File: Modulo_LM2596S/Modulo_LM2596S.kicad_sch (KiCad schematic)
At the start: 11 parts, among them U101 LM2596S-ADJ

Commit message: Footprint potenziometro (20/10/2022)
Ho assegnato la footprint al potenziometro, controllare se è corretto.
Il resto del circuito non è stato controllato
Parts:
- RV101: footprint (none) -> Potentiometer_THT:Potentiometer_Bourns_3299W_Vertical
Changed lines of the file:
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@@
       (effects (font (size 1.27 1.27)) (justify right))
     )
-    (property "Footprint" "" (id 2) (at 160.02 77.47 0)
+    (property "Footprint" "Potentiometer_THT:Potentiometer_Bourns_3299W_Vertical" (id 2) (at 160.02 77.47 0)
       (effects (font (size 1.27 1.27)) hide)
     )
@@
     )
     (path "/db17a703-a37d-4b79-9726-63333a30eb05"
-      (reference "RV101") (unit 1) (value "10k") (footprint "")
+      (reference "RV101") (unit 1) (value "10k") (footprint "Potentiometer_THT:Potentiometer_Bourns_3299W_Vertical")
     )
     (path "/329e714d-77d1-42d4-b688-ff586e973cc8"

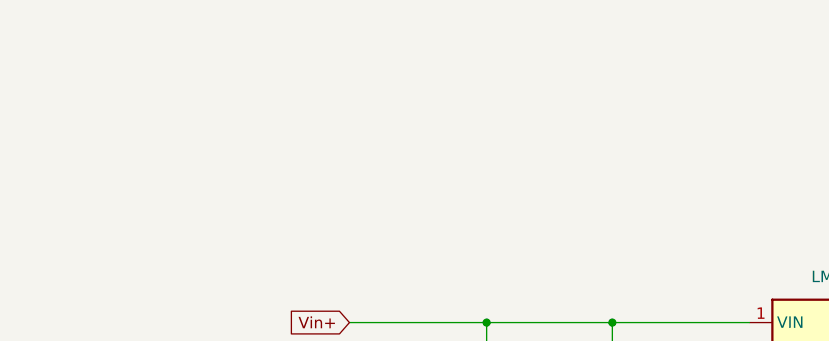
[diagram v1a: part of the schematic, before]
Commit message: Aggiunta di commento su potenziometro
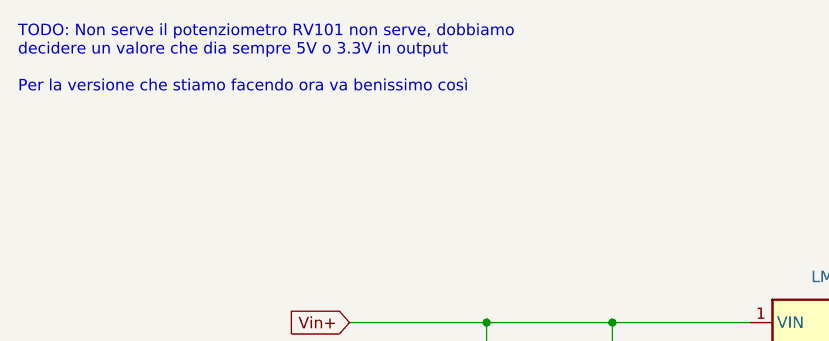
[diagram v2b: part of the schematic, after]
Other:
- note added: "TODO: Non serve il potenziometro RV101 non serve, dobbiamo decidere un valore che dia sempre 5V o 3.3V in output Per la versione che stiamo facendo ora va benissimo così"
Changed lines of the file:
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@@
     (stroke (width 0) (type default) (color 0 0 0 0))
+  )
+  (text "TODO: Non serve il potenziometro RV101 non serve, dobbiamo \ndecidere un valore che dia sempre 5V o 3.3V in output \n\nPer la versione che stiamo facendo ora va benissimo così"
+    (at 20.32 46.99 0)
+    (effects (font (size 1.27 1.27)) (justify left bottom))
   )
   (global_label "OUT+" (shape input) (at 193.04 73.66 0) (fields_autoplaced)

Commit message: Test delle metriche (22/10/2022)
Solo un test, non è finale o completo.
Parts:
- C101: footprint (none) -> Capacitor_SMD:CP_Elec_3x5.3
- C102: footprint (none) -> Capacitor_SMD:C_1812_4532Metric_Pad1.57x3.40mm_HandSolder
- R101: footprint (none) -> Resistor_SMD:R_0805_2012Metric_Pad1.20x1.40mm_HandSolder
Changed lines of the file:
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@@
       (effects (font (size 1.27 1.27)) (justify left))
     )
-    (property "Footprint" "" (id 2) (at 72.39 81.28 0)
+    (property "Footprint" "Capacitor_SMD:CP_Elec_3x5.3" (id 2) (at 72.39 81.28 0)
       (effects (font (size 1.27 1.27)) hide)
     )
@@
       (effects (font (size 1.27 1.27)) (justify left))
     )
-    (property "Footprint" "" (id 2) (at 158.242 86.36 90)
+    (property "Footprint" "Resistor_SMD:R_0805_2012Metric_Pad1.20x1.40mm_HandSolder" (id 2) (at 158.242 86.36 90)
       (effects (font (size 1.27 1.27)) hide)
     )
@@
       (effects (font (size 1.27 1.27)) (justify left))
     )
-    (property "Footprint" "" (id 2) (at 87.3252 85.09 0)
+    (property "Footprint" "Capacitor_SMD:C_1812_4532Metric_Pad1.57x3.40mm_HandSolder" (id 2) (at 87.3252 85.09 0)
       (effects (font (size 1.27 1.27)) hide)
     )
@@
     )
     (path "/36af99ba-44f3-4caf-a2f7-2f75678a02fb"
-      (reference "C101") (unit 1) (value "100uF") (footprint "")
+      (reference "C101") (unit 1) (value "100uF") (footprint "Capacitor_SMD:CP_Elec_3x5.3")
     )
     (path "/689c4dca-aa7d-493b-824b-0f528cf7fb1d"
-      (reference "C102") (unit 1) (value "1uF") (footprint "")
+      (reference "C102") (unit 1) (value "1uF") (footprint "Capacitor_SMD:C_1812_4532Metric_Pad1.57x3.40mm_HandSolder")
     )
     (path "/93b82181-0c21-4647-a6a8-8a9a0831c12f"
@@
     )
     (path "/664bdff7-aac1-4a8f-b1b1-4cc25c686d35"
-      (reference "R101") (unit 1) (value "330") (footprint "")
+      (reference "R101") (unit 1) (value "330") (footprint "Resistor_SMD:R_0805_2012Metric_Pad1.20x1.40mm_HandSolder")
     )
     (path "/8d177f27-30dc-4386-8473-ae66aa314cc6"

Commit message: Footprint (tentativo fallito)
23/10/2022 tentato di assegnare le footprint a tutti i componenti dello schema logico, ma senza successo
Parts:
- L101: footprint (none) -> Inductor_SMD:L_Bourns-SRU8028_8.0x8.0mm
- R102: footprint (none) -> Resistor_SMD:R_0805_2012Metric_Pad1.20x1.40mm_HandSolder
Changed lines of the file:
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@@
     (property "Reference" "L101" (id 0) (at 135.89 71.12 0))
     (property "Value" "47uH" (id 1) (at 135.89 73.66 0))
-    (property "Footprint" "" (id 2) (at 135.89 77.47 0)
+    (property "Footprint" "Inductor_SMD:L_Bourns-SRU8028_8.0x8.0mm" (id 2) (at 135.89 77.47 0)
       (effects (font (size 1.27 1.27)) hide)
     )
@@
       (effects (font (size 1.27 1.27)) (justify left))
     )
-    (property "Footprint" "" (id 2) (at 179.832 78.74 90)
+    (property "Footprint" "Resistor_SMD:R_0805_2012Metric_Pad1.20x1.40mm_HandSolder" (id 2) (at 179.832 78.74 90)
       (effects (font (size 1.27 1.27)) hide)
     )
@@
     )
     (path "/6d551d3c-151e-4aa5-b2c4-444cfcec29b2"
-      (reference "L101") (unit 1) (value "47uH") (footprint "")
+      (reference "L101") (unit 1) (value "47uH") (footprint "Inductor_SMD:L_Bourns-SRU8028_8.0x8.0mm")
     )
     (path "/664bdff7-aac1-4a8f-b1b1-4cc25c686d35"
@@
     )
     (path "/8d177f27-30dc-4386-8473-ae66aa314cc6"
-      (reference "R102") (unit 1) (value "1k") (footprint "")
+      (reference "R102") (unit 1) (value "1k") (footprint "Resistor_SMD:R_0805_2012Metric_Pad1.20x1.40mm_HandSolder")
     )
     (path "/db17a703-a37d-4b79-9726-63333a30eb05"

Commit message: LM2596S: creazione della scheda fisica
Selezione dei componenti e creazione del PCB.
TODO: Da mettere a posto le tracce @GiovanniRaseraF
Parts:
- removed D102: LED, symbol Device:LED
- removed R102: 1k, Resistor_SMD:R_0805_2012Metric_Pad1.20x1.40mm_HandSolder, symbol Device:R
- C101: footprint Capacitor_SMD:CP_Elec_3x5.3 -> Capacitor_SMD:CP_Elec_6.3x3.9
- C102: footprint Capacitor_SMD:C_1812_4532Metric_Pad1.57x3.40mm_HandSolder -> Capacitor_SMD:C_1206_3216Metric_Pad1.33x1.80mm_HandSolder
- C103: footprint (none) -> Capacitor_SMD:CP_Elec_6.3x3.9
- C104: footprint (none) -> Capacitor_SMD:C_1206_3216Metric_Pad1.33x1.80mm_HandSolder
- D101: footprint (none) -> Diode_SMD:D_SMB_Handsoldering
- L101: footprint Inductor_SMD:L_Bourns-SRU8028_8.0x8.0mm -> Inductor_SMD:L_Bourns_SRR1208_12.7x12.7mm
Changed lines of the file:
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@@
   (junction (at 146.05 77.47) (diameter 0) (color 0 0 0 0)
   )
-  (junction (at 181.61 91.44) (diameter 0) (color 0 0 0 0)
-  )
-  (junction (at 181.61 73.66) (diameter 0) (color 0 0 0 0)
-  )
   (junction (at 160.02 81.28) (diameter 0) (color 0 0 0 0)
   )
@@
     (stroke (width 0) (type default) (color 0 0 0 0))
   )
-  (wire (pts (xy 181.61 74.93) (xy 181.61 73.66))
-    (stroke (width 0) (type default) (color 0 0 0 0))
-  )
-  (wire (pts (xy 181.61 73.66) (xy 171.45 73.66))
+  (wire (pts (xy 171.45 73.66) (xy 193.04 73.66))
     (stroke (width 0) (type default) (color 0 0 0 0))
   )
@@
     (stroke (width 0) (type default) (color 0 0 0 0))
   )
-  (wire (pts (xy 181.61 82.55) (xy 181.61 83.82))
-    (stroke (width 0) (type default) (color 0 0 0 0))
-  )
   (wire (pts (xy 160.02 81.28) (xy 160.02 82.55))
     (stroke (width 0) (type default) (color 0 0 0 0))
@@
   )
   (wire (pts (xy 156.21 81.28) (xy 160.02 81.28))
-    (stroke (width 0) (type default) (color 0 0 0 0))
-  )
-  (wire (pts (xy 181.61 73.66) (xy 193.04 73.66))
     (stroke (width 0) (type default) (color 0 0 0 0))
   )
@@
       (effects (font (size 1.27 1.27)) (justify left))
     )
-    (property "Footprint" "Capacitor_SMD:CP_Elec_3x5.3" (id 2) (at 72.39 81.28 0)
+    (property "Footprint" "Capacitor_SMD:CP_Elec_6.3x3.9" (id 2) (at 72.39 81.28 0)
       (effects (font (size 1.27 1.27)) hide)
     )
@@
       (effects (font (size 1.27 1.27)) (justify left))
     )
-    (property "Footprint" "Capacitor_SMD:C_1812_4532Metric_Pad1.57x3.40mm_HandSolder" (id 2) (at 87.3252 85.09 0)
+    (property "Footprint" "Capacitor_SMD:C_1206_3216Metric_Pad1.33x1.80mm_HandSolder" (id 2) (at 87.3252 85.09 0)
       (effects (font (size 1.27 1.27)) hide)
     )
@@
     (property "Reference" "L101" (id 0) (at 135.89 71.12 0))
     (property "Value" "47uH" (id 1) (at 135.89 73.66 0))
-    (property "Footprint" "Inductor_SMD:L_Bourns-SRU8028_8.0x8.0mm" (id 2) (at 135.89 77.47 0)
+    (property "Footprint" "Inductor_SMD:L_Bourns_SRR1208_12.7x12.7mm" (id 2) (at 135.89 77.47 0)
       (effects (font (size 1.27 1.27)) hide)
     )
@@
       (effects (font (size 1.27 1.27)) (justify left))
     )
-    (property "Footprint" "" (id 2) (at 129.54 83.82 0)
+    (property "Footprint" "Diode_SMD:D_SMB_Handsoldering" (id 2) (at 129.54 83.82 0)
       (effects (font (size 1.27 1.27)) hide)
     )
     (property "Datasheet" "~" (id 3) (at 129.54 83.82 0)
-      (effects (font (size 1.27 1.27)) hide)
-    )
-    (pin "1")
-    (pin "2")
-  )
-  (symbol (lib_id "Device:LED") (at 181.61 87.63 90) (unit 1)
-    (in_bom yes) (on_board yes) (fields_autoplaced)
-    (property "Reference" "D102" (id 0) (at 185.42 87.9474 90)
-      (effects (font (size 1.27 1.27)) (justify right))
-    )
-    (property "Value" "LED" (id 1) (at 185.42 90.4874 90)
-      (effects (font (size 1.27 1.27)) (justify right))
-    )
-    (property "Footprint" "" (id 2) (at 181.61 87.63 0)
-      (effects (font (size 1.27 1.27)) hide)
-    )
-    (property "Datasheet" "~" (id 3) (at 181.61 87.63 0)
-      (effects (font (size 1.27 1.27)) hide)
-    )
-    (pin "1")
-    (pin "2")
-  )
-  (symbol (lib_id "Device:R") (at 181.61 78.74 0) (unit 1)
-    (in_bom yes) (on_board yes) (fields_autoplaced)
-    (property "Reference" "R102" (id 0) (at 184.15 77.4699 0)
-      (effects (font (size 1.27 1.27)) (justify left))
-    )
-    (property "Value" "1k" (id 1) (at 184.15 80.0099 0)
-      (effects (font (size 1.27 1.27)) (justify left))
-    )
-    (property "Footprint" "Resistor_SMD:R_0805_2012Metric_Pad1.20x1.40mm_HandSolder" (id 2) (at 179.832 78.74 90)
-      (effects (font (size 1.27 1.27)) hide)
-    )
-    (property "Datasheet" "~" (id 3) (at 181.61 78.74 0)
       (effects (font (size 1.27 1.27)) hide)
     )
@@
       (effects (font (size 1.27 1.27)) (justify left))
     )
-    (property "Footprint" "" (id 2) (at 146.05 81.28 0)
+    (property "Footprint" "Capacitor_SMD:CP_Elec_6.3x3.9" (id 2) (at 146.05 81.28 0)
       (effects (font (size 1.27 1.27)) hide)
     )
@@
       (effects (font (size 1.27 1.27)) (justify left))
     )
-    (property "Footprint" "" (id 2) (at 172.4152 85.09 0)
+    (property "Footprint" "Capacitor_SMD:C_1206_3216Metric_Pad1.33x1.80mm_HandSolder" (id 2) (at 172.4152 85.09 0)
       (effects (font (size 1.27 1.27)) hide)
     )
@@
     )
     (path "/36af99ba-44f3-4caf-a2f7-2f75678a02fb"
-      (reference "C101") (unit 1) (value "100uF") (footprint "Capacitor_SMD:CP_Elec_3x5.3")
+      (reference "C101") (unit 1) (value "100uF") (footprint "Capacitor_SMD:CP_Elec_6.3x3.9")
     )
     (path "/689c4dca-aa7d-493b-824b-0f528cf7fb1d"
-      (reference "C102") (unit 1) (value "1uF") (footprint "Capacitor_SMD:C_1812_4532Metric_Pad1.57x3.40mm_HandSolder")
+      (reference "C102") (unit 1) (value "1uF") (footprint "Capacitor_SMD:C_1206_3216Metric_Pad1.33x1.80mm_HandSolder")
     )
     (path "/93b82181-0c21-4647-a6a8-8a9a0831c12f"
-      (reference "C103") (unit 1) (value "220uF") (footprint "")
+      (reference "C103") (unit 1) (value "220uF") (footprint "Capacitor_SMD:CP_Elec_6.3x3.9")
     )
     (path "/f8d84435-5a6f-4245-9c39-c6eb9e5c9a54"
-      (reference "C104") (unit 1) (value "1uF") (footprint "")
+      (reference "C104") (unit 1) (value "1uF") (footprint "Capacitor_SMD:C_1206_3216Metric_Pad1.33x1.80mm_HandSolder")
     )
     (path "/78ac60e5-1656-4859-938e-3eeb9bf3adb1"
-      (reference "D101") (unit 1) (value "SS34") (footprint "")
-    )
-    (path "/8575f82e-c20e-489b-a776-f071d94a1f0d"
-      (reference "D102") (unit 1) (value "LED") (footprint "")
+      (reference "D101") (unit 1) (value "SS34") (footprint "Diode_SMD:D_SMB_Handsoldering")
     )
     (path "/6d551d3c-151e-4aa5-b2c4-444cfcec29b2"
-      (reference "L101") (unit 1) (value "47uH") (footprint "Inductor_SMD:L_Bourns-SRU8028_8.0x8.0mm")
+      (reference "L101") (unit 1) (value "47uH") (footprint "Inductor_SMD:L_Bourns_SRR1208_12.7x12.7mm")
     )
     (path "/664bdff7-aac1-4a8f-b1b1-4cc25c686d35"
       (reference "R101") (unit 1) (value "330") (footprint "Resistor_SMD:R_0805_2012Metric_Pad1.20x1.40mm_HandSolder")
     )
-    (path "/8d177f27-30dc-4386-8473-ae66aa314cc6"
-      (reference "R102") (unit 1) (value "1k") (footprint "Resistor_SMD:R_0805_2012Metric_Pad1.20x1.40mm_HandSolder")
-    )
     (path "/db17a703-a37d-4b79-9726-63333a30eb05"

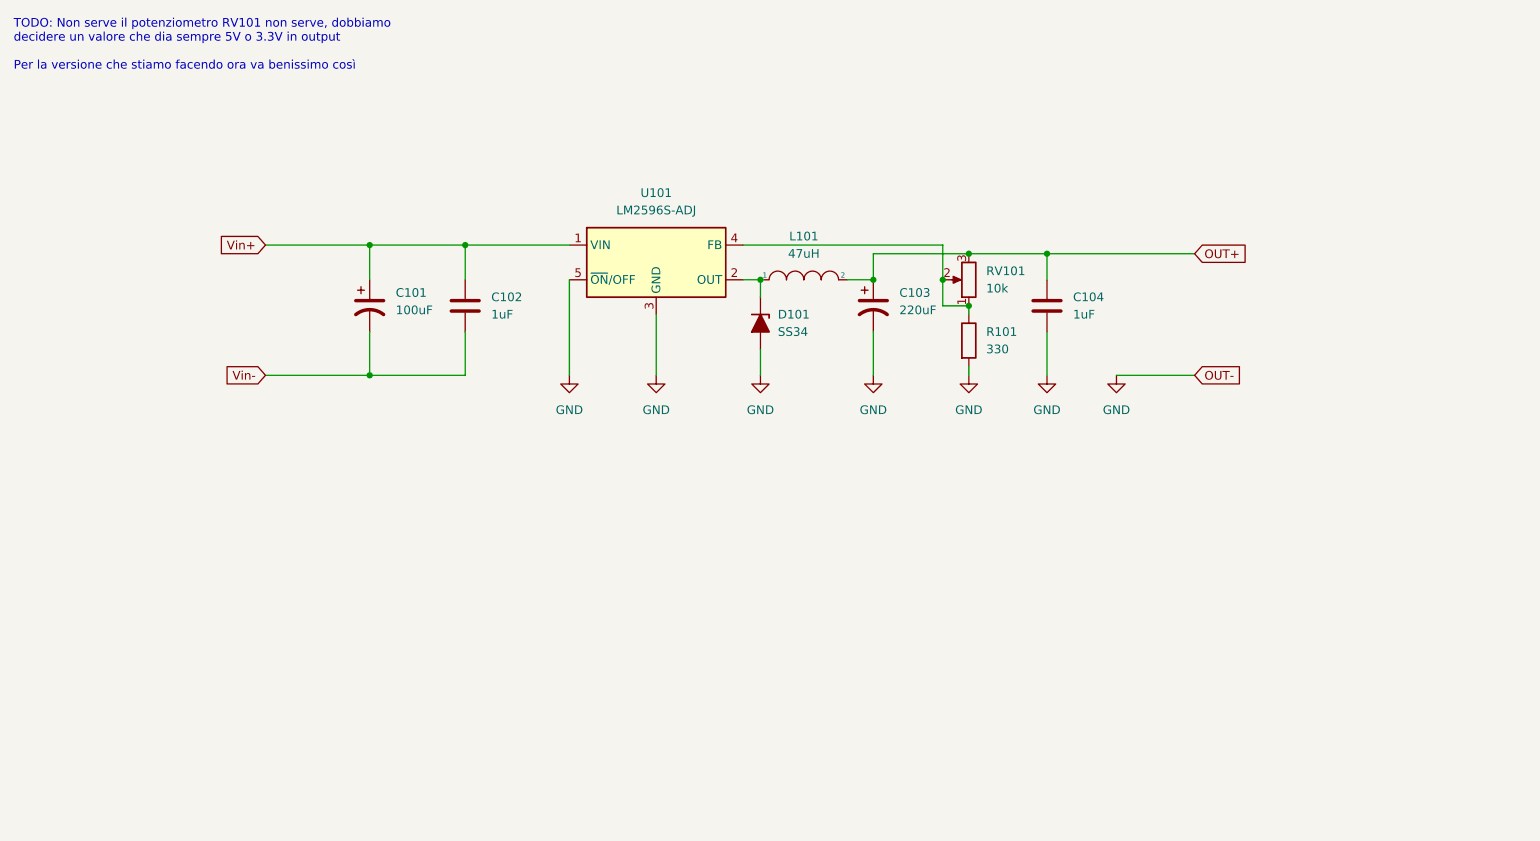
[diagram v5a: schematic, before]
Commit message: LM2596: Finito di tirare le tracce
Tirato le tracce e il piano di GND
Inserito io MountPad ed i punti di solder dei cavi di input e output
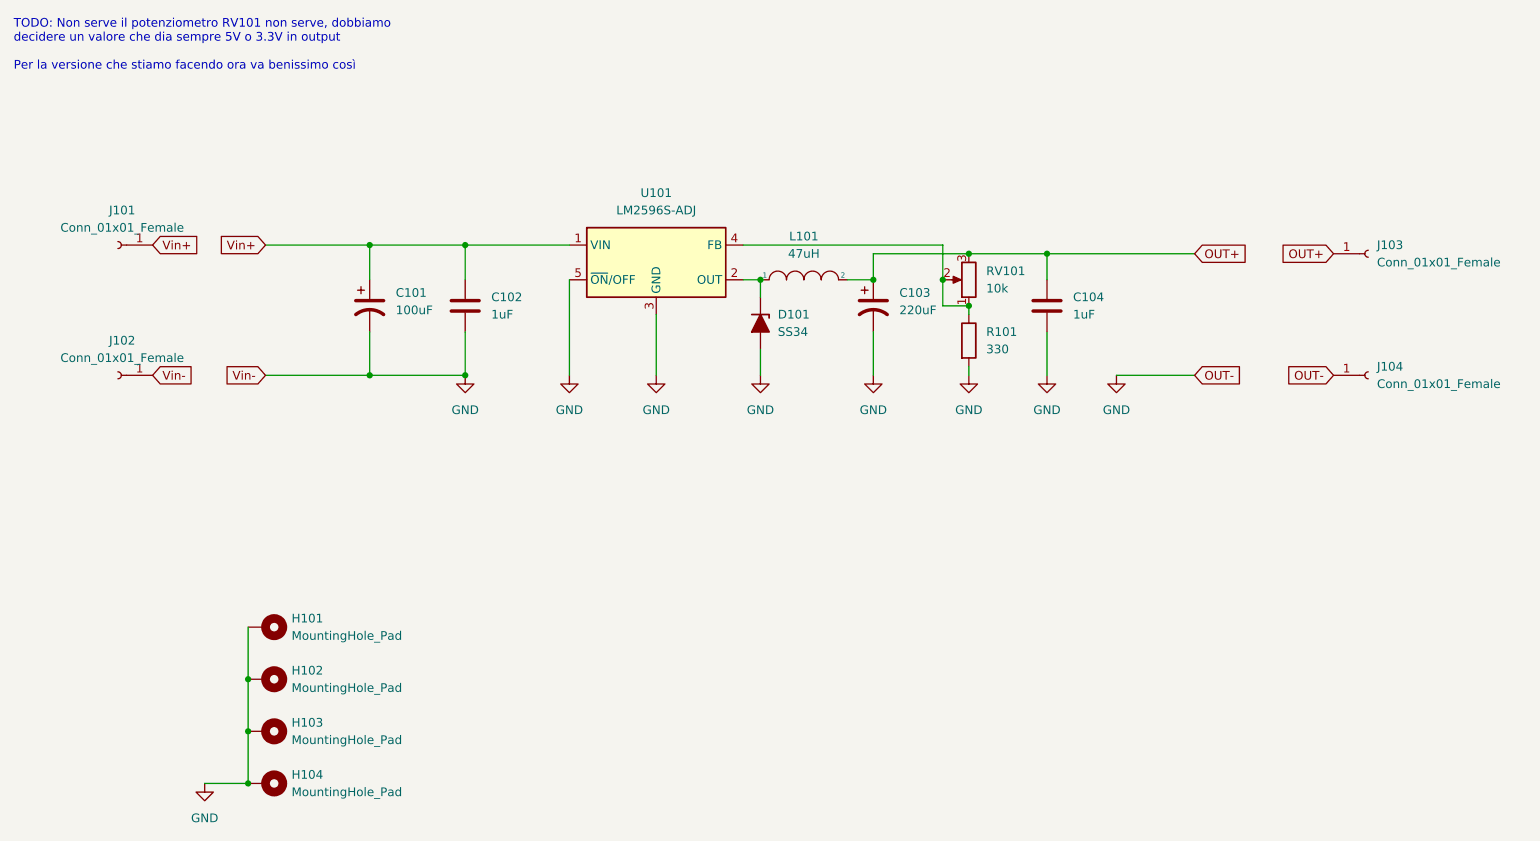
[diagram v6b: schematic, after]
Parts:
- added H101, H102, H103, H104: MountingHole_Pad, MountingHole:MountingHole_2.2mm_M2_Pad_Via, symbol Mechanical:MountingHole_Pad
- added J101, J102, J103, J104: Conn_01x01_Female, Connector_Wire:SolderWirePad_1x01_SMD_1x2mm, symbol Connector:Conn_01x01_Female
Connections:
- net Vin- is gone; now on net GND: C101.2, C102.2
- net GND: now also H101.1, H102.1, H103.1, H104.1, J102.1 (Pin_1), J104.1 (Pin_1)
- net OUT+: now also J103.1 (Pin_1)
- net Vin+: now also J101.1 (Pin_1)
